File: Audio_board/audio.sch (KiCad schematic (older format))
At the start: 21 parts, among them J2 AudioJack2_Ground, J4 Conn_01x04, U2 PCM5121, U3 Audio_amp_OEP30W, U4 Audio_amp_OEP30Wx2

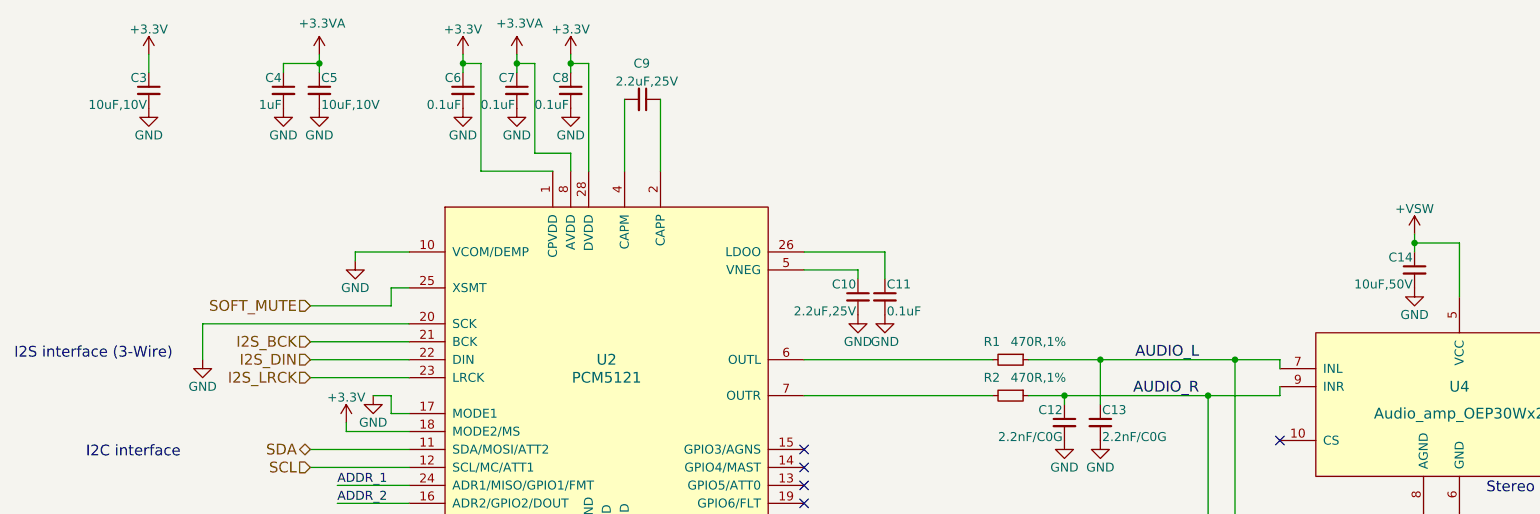
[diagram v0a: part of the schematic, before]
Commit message: Fix component values > pick n place convention
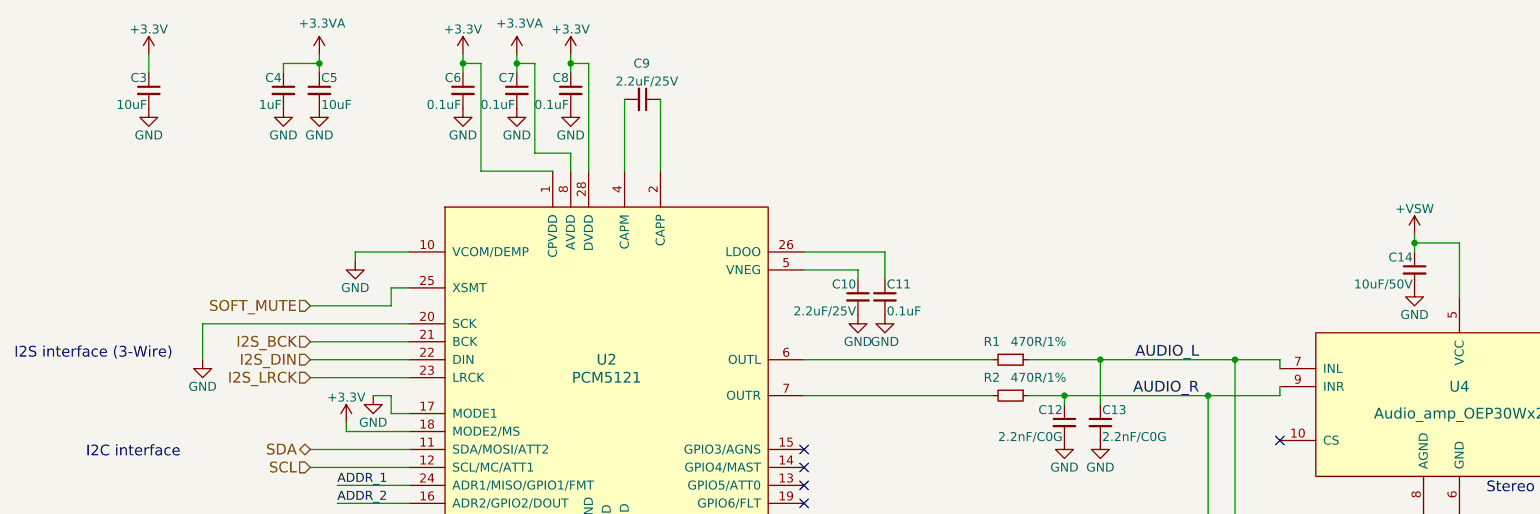
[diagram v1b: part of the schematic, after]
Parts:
- C10, C9: value 2.2uF,25V -> 2.2uF/25V
- C14: value 10uF,50V -> 10uF/50V
- C3, C5: value 10uF,10V -> 10uF
- R1, R2: value 470R,1% -> 470R/1%
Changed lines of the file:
@@
 P 1500 1250
 F 0 "C3" H 1510 1320 50  0000 L CNN
-F 1 "10uF,10V" H 1510 1170 50  0000 L CNN
+F 1 "10uF" H 1510 1170 50  0000 L CNN
 F 2 "Capacitor_SMD:C_0805_2012Metric" H 1500 1250 50  0001 C CNN
 F 3 "" H 1500 1250 50  0001 C CNN
@@
 P 4250 1300
 F 0 "C9" V 4050 1250 50  0000 L CNN
-F 1 "2.2uF,25V" V 4150 1150 50  0000 L CNN
+F 1 "2.2uF/25V" V 4150 1150 50  0000 L CNN
 F 2 "Capacitor_SMD:C_0603_1608Metric" H 4250 1300 50  0001 C CNN
 F 3 "" H 4250 1300 50  0001 C CNN
@@
 P 5450 2400
 F 0 "C10" H 5460 2470 50  0000 L CNN
-F 1 "2.2uF,25V" H 5460 2320 50  0000 L CNN
+F 1 "2.2uF/25V" H 5460 2320 50  0000 L CNN
 F 2 "Capacitor_SMD:C_0603_1608Metric" H 5450 2400 50  0001 C CNN
 F 3 "" H 5450 2400 50  0001 C CNN
@@
 P 6300 2750
 F 0 "R1" V 6200 2600 50  0000 L CNN
-F 1 "470R,1%" V 6200 2750 50  0000 L CNN
+F 1 "470R/1%" V 6200 2750 50  0000 L CNN
 F 2 "Resistor_SMD:R_0603_1608Metric" H 6300 2750 50  0001 C CNN
 F 3 "" H 6300 2750 50  0001 C CNN
@@
 P 6300 2950
 F 0 "R2" V 6200 2800 50  0000 L CNN
-F 1 "470R,1%" V 6200 2950 50  0000 L CNN
+F 1 "470R/1%" V 6200 2950 50  0000 L CNN
 F 2 "Resistor_SMD:R_0603_1608Metric" H 6300 2950 50  0001 C CNN
 F 3 "" H 6300 2950 50  0001 C CNN
@@
 P 8550 2250
 F 0 "C14" H 8560 2320 50  0000 L CNN
-F 1 "10uF,50V" H 8560 2170 50  0000 L CNN
+F 1 "10uF/50V" H 8560 2170 50  0000 L CNN
 F 2 "Capacitor_SMD:C_1206_3216Metric" H 8550 2250 50  0001 C CNN
 F 3 "" H 8550 2250 50  0001 C CNN
@@
 P 2450 1250
 F 0 "C5" H 2460 1320 50  0000 L CNN
-F 1 "10uF,10V" H 2460 1170 50  0000 L CNN
+F 1 "10uF" H 2460 1170 50  0000 L CNN
 F 2 "Capacitor_SMD:C_0805_2012Metric" H 2450 1250 50  0001 C CNN
 F 3 "" H 2450 1250 50  0001 C CNN

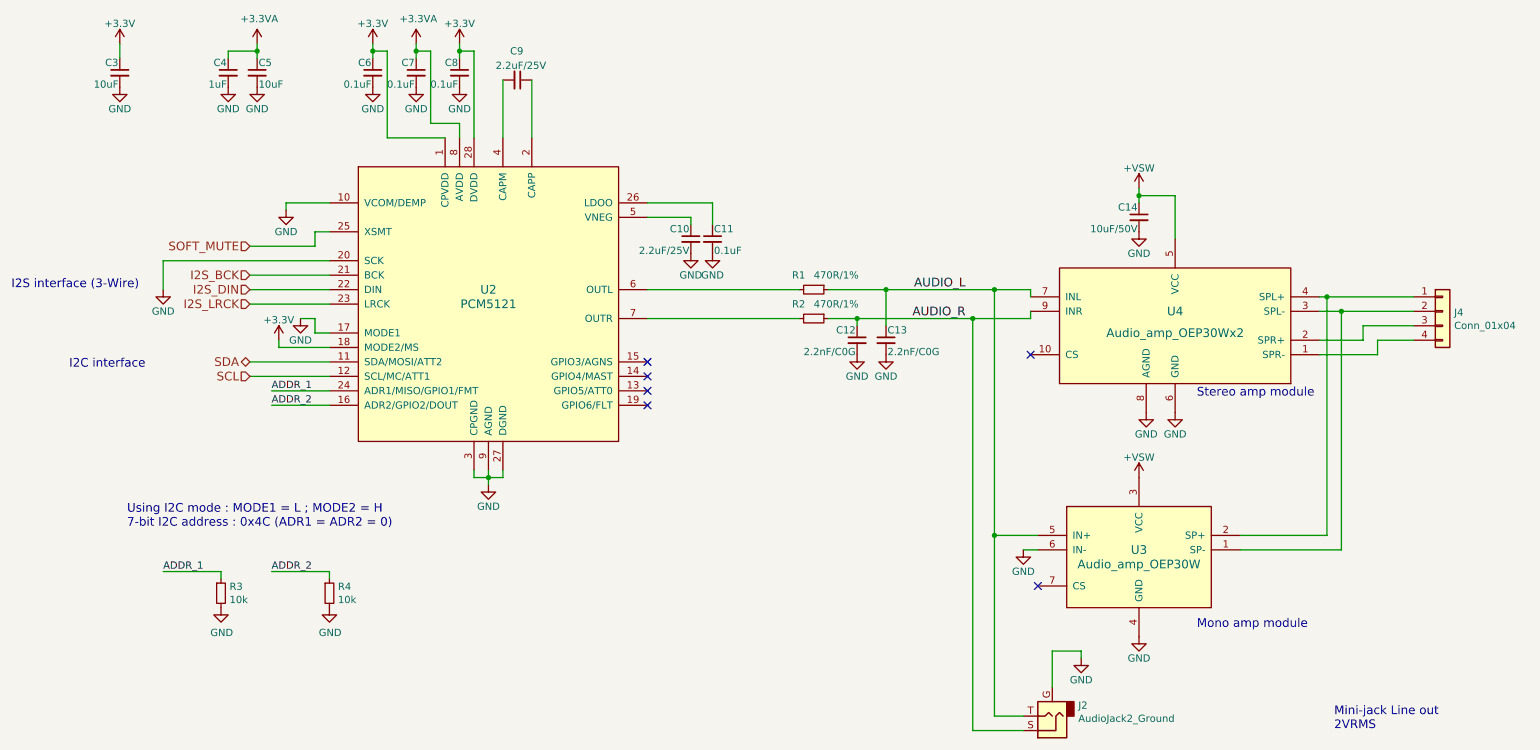
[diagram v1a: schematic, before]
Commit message: update gerber and add current sensor doc
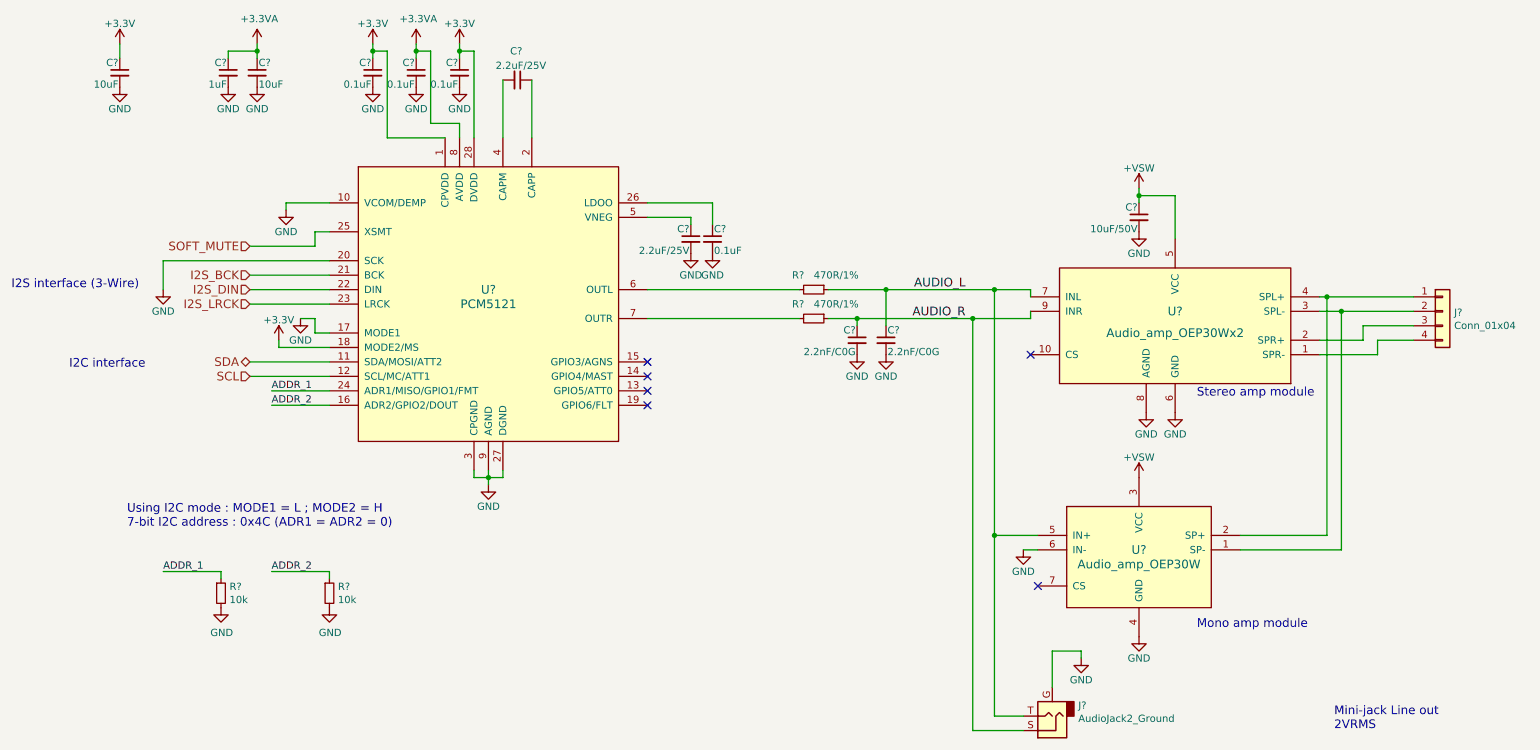
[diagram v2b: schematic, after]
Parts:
- renumbered C8 to C?, C7 to C?, C6 to C?, C3 to C?, C4 to C?, C9 to C?, C11 to C?, C10 to C?, C13 to C?, C12 to C?, C14 to C?, C5 to C?, J2 to J?, J4 to J?, R1 to R?, R2 to R?, R3 to R?, R4 to R?, U3 to U?, U4 to U?, U2 to U?
